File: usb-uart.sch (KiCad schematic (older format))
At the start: 11 parts

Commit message: sch: Add misc doc texts
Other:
- note added: "Connect both USB data pins despite\nthe stubs it will create: at USB 2.0\nspeeds, this is not really an issue"
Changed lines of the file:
@@
 Wire Wire Line
 	3150 4550 3300 4550
+Text Notes 3500 5100 0    50   ~ 0
+Connect both USB data pins despite\nthe stubs it will create: at USB 2.0\nspeeds, this is not really an issue
 $EndSCHEMATC

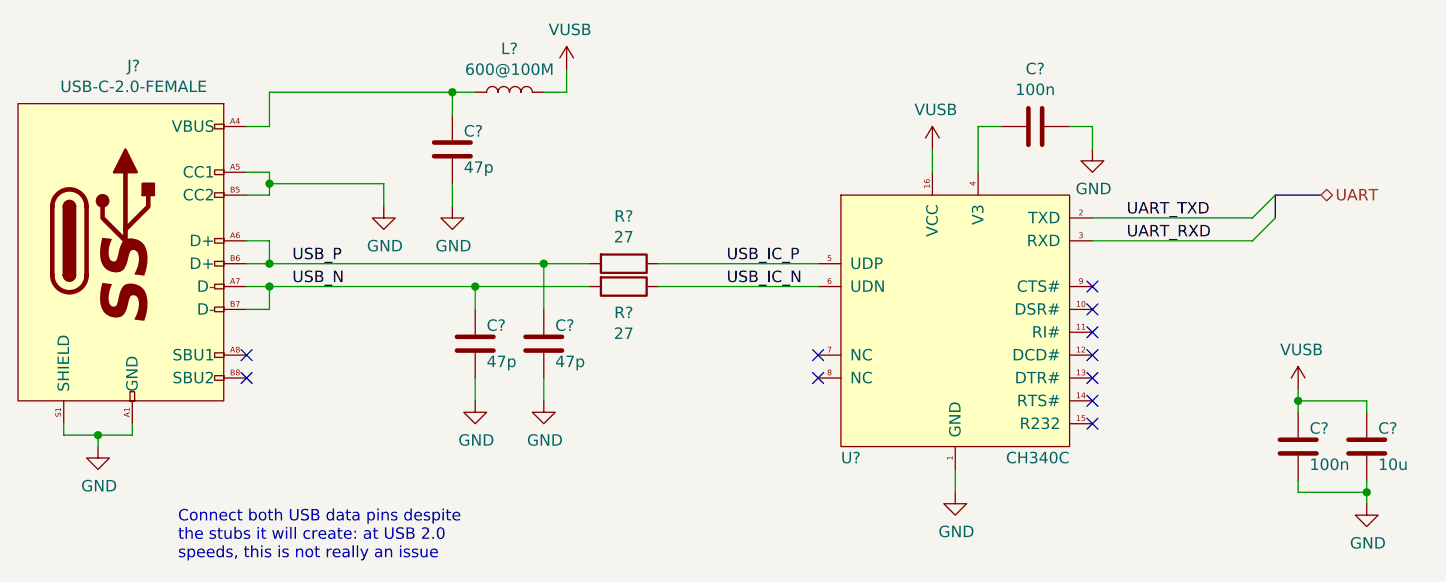
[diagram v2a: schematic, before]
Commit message: sch: Replace regular symbols with small variant
Done for most capacitors and resistors
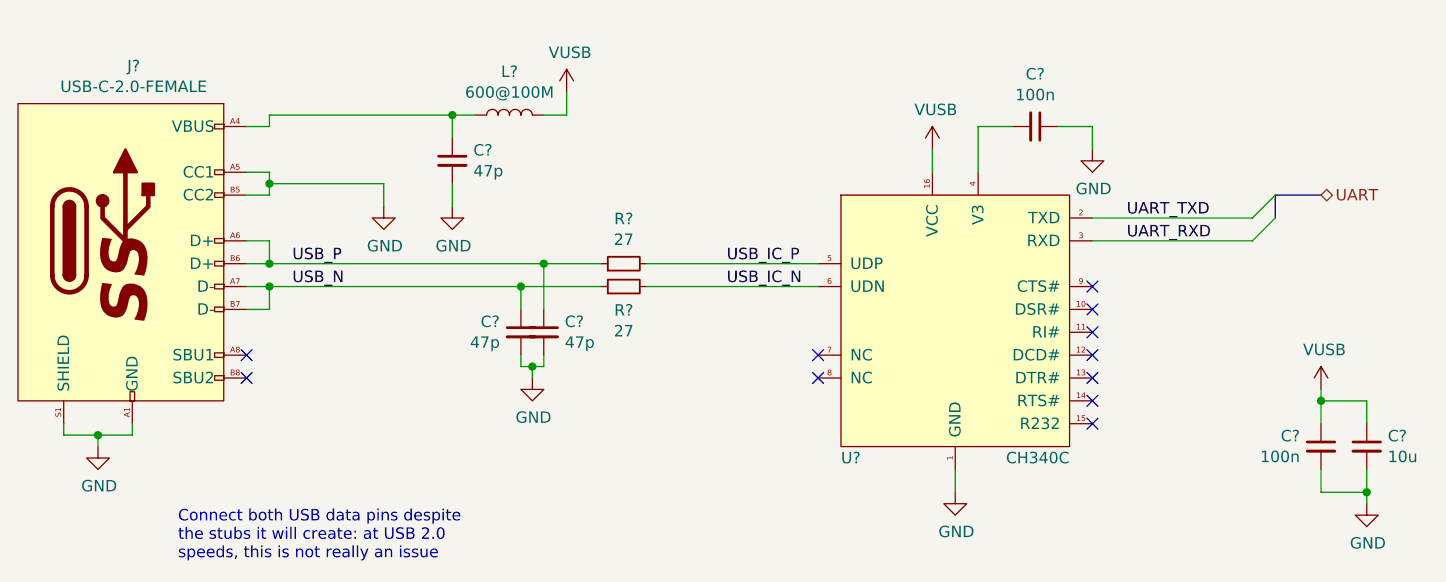
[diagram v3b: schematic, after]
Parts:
- removed C? (x2): 100n, symbol Device:C
- removed C? (x3): 47p, symbol Device:C
- removed C?: 10u, symbol Device:C
- removed R? (x2): 27, symbol Device:R
- added C? (x3): 47p, symbol Device:C_Small
- added C? (x2): 100n, symbol Device:C_Small
- added C?: 10u, symbol Device:C_Small
- added R? (x2): 27, symbol Device:R_Small
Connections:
- net GND: now also C?.1, C?.2, C?.2, C?.2, C?.2, C?.2
- net USB_IC_N: now also R?.2
- net USB_IC_P: now also R?.2
- net USB_N: now also C?.1, R?.1
- net USB_P: now also C?.1, R?.1
- net VUSB: now also C?.1, C?.1
- net at U?.4 (V3): now also C?.2
- net at J?.A4 (VBUS), J?.A9 (VBUS), J?.B4 (VBUS)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: now also C?.1
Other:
- moved on the sheet: L?
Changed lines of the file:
@@
 Wire Wire Line
 	6800 3300 6800 3400
-$Comp
-L Device:C C?
-U 1 1 5D27AF80
-P 7250 3200
-F 0 "C?" V 6998 3200 50  0000 C CNN
-F 1 "100n" V 7089 3200 50  0000 C CNN
-F 2 "" H 7288 3050 50  0001 C CNN
-F 3 "~" H 7250 3200 50  0001 C CNN
-	1    7250 3200
-	0    1    1    0
-$EndComp
 Wire Wire Line
 	7000 3400 7000 3200
-Wire Wire Line
-	7000 3200 7100 3200
 $Comp
 L power:GND #PWR?
@@
 	1    0    0    -1
 $EndComp
-Wire Wire Line
-	7400 3200 7500 3200
 Wire Wire Line
 	7500 3200 7500 3300
@@
 	1    0    0    -1
 $EndComp
-$Comp
-L Device:R R?
-U 1 1 5D27BD30
-P 5450 3800
-F 0 "R?" V 5243 3800 50  0000 C CNN
-F 1 "27" V 5334 3800 50  0000 C CNN
-F 2 "" V 5380 3800 50  0001 C CNN
-F 3 "~" H 5450 3800 50  0001 C CNN
-	1    5450 3800
-	0    1    1    0
-$EndComp
-$Comp
-L Device:R R?
-U 1 1 5D27BE5B
-P 5450 3900
-F 0 "R?" V 5565 3900 50  0000 C CNN
-F 1 "27" V 5656 3900 50  0000 C CNN
-F 2 "" V 5380 3900 50  0001 C CNN
-F 3 "~" H 5450 3900 50  0001 C CNN
-	1    5450 3900
-	0    1    1    0
-$EndComp
-Wire Wire Line
-	5600 3800 6300 3800
-Wire Wire Line
-	6300 3900 5600 3900
-Wire Wire Line
-	5300 3800 5100 3800
+Wire Wire Line
+	5550 3800 6300 3800
+Wire Wire Line
+	6300 3900 5550 3900
+Wire Wire Line
+	5350 3800 5100 3800
 Wire Wire Line
 	3800 3900 3900 3900
@@
 	3900 4000 3800 4000
 Connection ~ 3900 3900
-Wire Wire Line
-	3900 3900 4800 3900
 Text Label 5900 3800 0    50   ~ 0
 USB_IC_P
@@
 NoConn ~ 7500 4400
 NoConn ~ 7500 4500
-$Comp
-L Device:C C?
-U 1 1 5D27E126
-P 5100 4150
-F 0 "C?" H 5050 4100 50  0000 R TNN
-F 1 "47p" H 5050 4200 50  0000 R BNN
-F 2 "" H 5138 4000 50  0001 C CNN
-F 3 "~" H 5100 4150 50  0001 C CNN
-	1    5100 4150
-	-1   0    0    1
-$EndComp
-$Comp
-L Device:C C?
-U 1 1 5D27E3AF
-P 4800 4150
-F 0 "C?" H 4750 4100 50  0000 R TNN
-F 1 "47p" H 4750 4200 50  0000 R BNN
-F 2 "" H 4838 4000 50  0001 C CNN
-F 3 "~" H 4800 4150 50  0001 C CNN
-	1    4800 4150
-	-1   0    0    1
-$EndComp
 Wire Wire Line
 	5100 4000 5100 3800
@@
 	5100 3800 3900 3800
 Wire Wire Line
-	4800 4000 4800 3900
-Connection ~ 4800 3900
-Wire Wire Line
-	4800 3900 5300 3900
+	5000 4000 5000 3900
 $Comp
 L power:GND #PWR?
 U 1 1 5D27ED1B
-P 5100 4400
-F 0 "#PWR?" H 5100 4150 50  0001 C CNN
-F 1 "GND" H 5105 4227 50  0000 C CNN
-F 2 "" H 5100 4400 50  0001 C CNN
-F 3 "" H 5100 4400 50  0001 C CNN
-	1    5100 4400
-	1    0    0    -1
-$EndComp
-$Comp
-L power:GND #PWR?
-U 1 1 5D27ED34
-P 4800 4400
-F 0 "#PWR?" H 4800 4150 50  0001 C CNN
-F 1 "GND" H 4805 4227 50  0000 C CNN
-F 2 "" H 4800 4400 50  0001 C CNN
-F 3 "" H 4800 4400 50  0001 C CNN
-	1    4800 4400
-	1    0    0    -1
-$EndComp
-Wire Wire Line
-	4800 4300 4800 4400
-Wire Wire Line
-	5100 4300 5100 4400
+P 5050 4300
+F 0 "#PWR?" H 5050 4050 50  0001 C CNN
+F 1 "GND" H 5055 4127 50  0000 C CNN
+F 2 "" H 5050 4300 50  0001 C CNN
+F 3 "" H 5050 4300 50  0001 C CNN
+	1    5050 4300
+	1    0    0    -1
+$EndComp
+Wire Wire Line
+	5000 4200 5000 4250
+Wire Wire Line
+	5100 4200 5100 4250
 Wire Wire Line
 	3300 4500 3300 4550
@@
 L Device:L L?
 U 1 1 5D2813FA
-P 4950 3050
+P 4950 3150
 AR Path="/5C7D0D1E/5C7D3CAF/5D2813FA" Ref="L?"  Part="1"
 AR Path="/5C7D0D1E/5C7D3CB2/5D2813FA" Ref="L?"  Part="1"
 AR Path="/5D2774DB/5D2813FA" Ref="L?"  Part="1"
-F 0 "L?" V 5140 3050 50  0000 C CNN
-F 1 "600@100M" V 5049 3050 50  0000 C CNN
-F 2 "" H 4950 3050 50  0001 C CNN
-F 3 "~" H 4950 3050 50  0001 C CNN
-	1    4950 3050
+F 0 "L?" V 5140 3150 50  0000 C CNN
+F 1 "600@100M" V 5049 3150 50  0000 C CNN
+F 2 "" H 4950 3150 50  0001 C CNN
+F 3 "~" H 4950 3150 50  0001 C CNN
+	1    4950 3150
 	0    -1   -1   0
 $EndComp
-$Comp
-L Device:C C?
-U 1 1 5D281882
-P 4700 3300
-F 0 "C?" H 4650 3250 50  0000 R TNN
-F 1 "47p" H 4650 3350 50  0000 R BNN
-F 2 "" H 4738 3150 50  0001 C CNN
-F 3 "~" H 4700 3300 50  0001 C CNN
-	1    4700 3300
-	-1   0    0    1
-$EndComp
-Wire Wire Line
-	3900 3200 3900 3050
-Wire Wire Line
-	3900 3050 4700 3050
+Wire Wire Line
+	3900 3200 3900 3150
 Wire Wire Line
 	3800 3200 3900 3200
-Wire Wire Line
-	4700 3150 4700 3050
-Connection ~ 4700 3050
-Wire Wire Line
-	4700 3050 4800 3050
 $Comp
 L power:GND #PWR?
@@
 L pimouss-motherboard:VUSB #PWR?
 U 1 1 5D2857EF
-P 5200 2950
-F 0 "#PWR?" H 5200 2800 50  0001 C CNN
-F 1 "VUSB" H 5215 3123 50  0000 C CNN
-F 2 "" H 5200 2950 50  0001 C CNN
-F 3 "" H 5200 2950 50  0001 C CNN
-	1    5200 2950
-	1    0    0    -1
-$EndComp
-Wire Wire Line
-	5100 3050 5200 3050
-Wire Wire Line
-	5200 3050 5200 2950
-$Comp
-L Device:C C?
-U 1 1 5D2868CF
-P 8700 4600
-F 0 "C?" H 8650 4550 50  0000 R TNN
-F 1 "10u" H 8650 4650 50  0000 R BNN
-F 2 "" H 8738 4450 50  0001 C CNN
-F 3 "~" H 8700 4600 50  0001 C CNN
-	1    8700 4600
-	-1   0    0    1
-$EndComp
-$Comp
-L Device:C C?
-U 1 1 5D2868D6
-P 8400 4600
-F 0 "C?" H 8350 4550 50  0000 R TNN
-F 1 "100n" H 8350 4650 50  0000 R BNN
-F 2 "" H 8438 4450 50  0001 C CNN
-F 3 "~" H 8400 4600 50  0001 C CNN
-	1    8400 4600
-	-1   0    0    1
-$EndComp
+P 5200 3050
+F 0 "#PWR?" H 5200 2900 50  0001 C CNN
+F 1 "VUSB" H 5215 3223 50  0000 C CNN
+F 2 "" H 5200 3050 50  0001 C CNN
+F 3 "" H 5200 3050 50  0001 C CNN
+	1    5200 3050
+	1    0    0    -1
+$EndComp
+Wire Wire Line
+	5100 3150 5200 3150
+Wire Wire Line
+	5200 3150 5200 3050
 $Comp
 L pimouss-motherboard:VUSB #PWR?
 U 1 1 5D286FE7
-P 8400 4350
-F 0 "#PWR?" H 8400 4200 50  0001 C CNN
-F 1 "VUSB" H 8415 4523 50  0000 C CNN
-F 2 "" H 8400 4350 50  0001 C CNN
-F 3 "" H 8400 4350 50  0001 C CNN
-	1    8400 4350
+P 8500 4350
+F 0 "#PWR?" H 8500 4200 50  0001 C CNN
+F 1 "VUSB" H 8515 4523 50  0000 C CNN
+F 2 "" H 8500 4350 50  0001 C CNN
+F 3 "" H 8500 4350 50  0001 C CNN
+	1    8500 4350
 	1    0    0    -1
 $EndComp
@@
 $EndComp
 Wire Wire Line
-	8400 4350 8400 4400
-Wire Wire Line
-	8400 4400 8700 4400
-Wire Wire Line
-	8700 4400 8700 4450
-Connection ~ 8400 4400
-Wire Wire Line
-	8400 4400 8400 4450
-Wire Wire Line
-	8400 4750 8400 4800
-Wire Wire Line
-	8400 4800 8700 4800
+	8500 4350 8500 4400
+Wire Wire Line
+	8500 4400 8700 4400
+Wire Wire Line
+	8700 4400 8700 4500
+Connection ~ 8500 4400
+Wire Wire Line
+	8500 4400 8500 4500
+Wire Wire Line
+	8500 4700 8500 4800
+Wire Wire Line
+	8500 4800 8700 4800
 Wire Wire Line
 	8700 4800 8700 4850
 Wire Wire Line
-	8700 4750 8700 4800
+	8700 4700 8700 4800
 Connection ~ 8700 4800
 Wire Wire Line
@@
 Text Notes 3500 5100 0    50   ~ 0
 Connect both USB data pins despite\nthe stubs it will create: at USB 2.0\nspeeds, this is not really an issue
+$Comp
+L Device:R_Small R?
+U 1 1 5D489A44
+P 5450 3800
+F 0 "R?" V 5646 3800 50  0000 C CNN
+F 1 "27" V 5555 3800 50  0000 C CNN
+F 2 "" H 5450 3800 50  0001 C CNN
+F 3 "~" H 5450 3800 50  0001 C CNN
+	1    5450 3800
+	0    -1   -1   0
+$EndComp
+$Comp
+L Device:C_Small C?
+U 1 1 5D48AA53
+P 4700 3350
+F 0 "C?" H 4792 3396 50  0000 L CNN
+F 1 "47p" H 4792 3305 50  0000 L CNN
+F 2 "" H 4700 3350 50  0001 C CNN
+F 3 "~" H 4700 3350 50  0001 C CNN
+	1    4700 3350
+	1    0    0    -1
+$EndComp
+Wire Wire Line
+	4700 3250 4700 3150
+Wire Wire Line
+	3900 3150 4700 3150
+Connection ~ 4700 3150
+Wire Wire Line
+	4700 3150 4800 3150
+$Comp
+L Device:R_Small R?
+U 1 1 5D491922
+P 5450 3900
+F 0 "R?" V 5346 3900 50  0000 C CNN
+F 1 "27" V 5255 3900 50  0000 C CNN
+F 2 "" H 5450 3900 50  0001 C CNN
+F 3 "~" H 5450 3900 50  0001 C CNN
+	1    5450 3900
+	0    -1   -1   0
+$EndComp
+$Comp
+L Device:C_Small C?
+U 1 1 5D493D2D
+P 5100 4100
+F 0 "C?" H 5192 4146 50  0000 L CNN
+F 1 "47p" H 5192 4055 50  0000 L CNN
+F 2 "" H 5100 4100 50  0001 C CNN
+F 3 "~" H 5100 4100 50  0001 C CNN
+	1    5100 4100
+	1    0    0    -1
+$EndComp
+$Comp
+L Device:C_Small C?
+U 1 1 5D495256
+P 5000 4100
+F 0 "C?" H 4908 4146 50  0000 R CNN
+F 1 "47p" H 4908 4055 50  0000 R CNN
+F 2 "" H 5000 4100 50  0001 C CNN
+F 3 "~" H 5000 4100 50  0001 C CNN
+	1    5000 4100
+	1    0    0    -1
+$EndComp
+Connection ~ 5000 3900
+Wire Wire Line
+	5000 3900 5350 3900
+Wire Wire Line
+	3900 3900 5000 3900
+Wire Wire Line
+	5000 4250 5050 4250
+Wire Wire Line
+	5050 4250 5050 4300
+Connection ~ 5050 4250
+Wire Wire Line
+	5050 4250 5100 4250
+$Comp
+L Device:C_Small C?
+U 1 1 5D4A0412
+P 7250 3200
+F 0 "C?" V 7021 3200 50  0000 C CNN
+F 1 "100n" V 7112 3200 50  0000 C CNN
+F 2 "" H 7250 3200 50  0001 C CNN
+F 3 "~" H 7250 3200 50  0001 C CNN
+	1    7250 3200
+	0    1    1    0
+$EndComp
+Wire Wire Line
+	7000 3200 7150 3200
+Wire Wire Line
+	7350 3200 7500 3200
+$Comp
+L Device:C_Small C?
+U 1 1 5D4A5872
+P 8500 4600
+F 0 "C?" H 8408 4646 50  0000 R CNN
+F 1 "100n" H 8408 4555 50  0000 R CNN
+F 2 "" H 8500 4600 50  0001 C CNN
+F 3 "~" H 8500 4600 50  0001 C CNN
+	1    8500 4600
+	1    0    0    -1
+$EndComp
+$Comp
+L Device:C_Small C?
+U 1 1 5D4A64DB
+P 8700 4600
+F 0 "C?" H 8792 4646 50  0000 L CNN
+F 1 "10u" H 8792 4555 50  0000 L CNN
+F 2 "" H 8700 4600 50  0001 C CNN
+F 3 "~" H 8700 4600 50  0001 C CNN
+	1    8700 4600
+	1    0    0    -1
+$EndComp
 $EndSCHEMATC

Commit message: sch: Remove ALL busses since kicad's support is broken
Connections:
- net UART_RXD renamed RXD
- net UART_TXD renamed TXD
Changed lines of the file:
@@
 	8200 3700 7500 3700
 Text Label 7650 3600 0    50   ~ 0
-UART_TXD
+TXD
 Text Label 7650 3700 0    50   ~ 0
-UART_RXD
-Wire Bus Line
-	8300 3600 8300 3500
-Wire Bus Line
-	8300 3500 8500 3500
-Entry Wire Line
-	8200 3600 8300 3500
-Entry Wire Line
-	8200 3700 8300 3600
-Text HLabel 8500 3500 2    50   BiDi ~ 0
-UART
+RXD
 Wire Wire Line
 	3900 3450 4400 3450
@@
 	1    0    0    -1
 $EndComp
+Text HLabel 8200 3600 2    50   Output ~ 0
+TXD
+Text HLabel 8200 3700 2    50   Input ~ 0
+RXD
 $EndSCHEMATC

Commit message: sch: Make ERC happy with dummy power outputs
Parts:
- added DS?: DummySupply, symbol pimouss-motherboard:DummySupply
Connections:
- net VUSB: now also DS?.~ (Dummy)
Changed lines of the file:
@@
 Text HLabel 8200 3700 2    50   Input ~ 0
 RXD
+$Comp
+L pimouss-motherboard:DummySupply DS?
+U 1 1 5E40E77B
+P 5200 3150
+F 0 "DS?" H 5200 3150 50  0001 C CNN
+F 1 "DummySupply" H 5200 3150 50  0001 C CNN
+F 2 "" H 5200 3150 50  0001 C CNN
+F 3 "" H 5200 3150 50  0001 C CNN
+	1    5200 3150
+	0    1    1    0
+$EndComp
+Connection ~ 5200 3150
 $EndSCHEMATC

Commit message: sch: Annotate & associate symbols with footprints
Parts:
- removed DS?: DummySupply, symbol pimouss-motherboard:DummySupply
- C34, C35, C36, C37, C38, C39: renamed from C?; footprint (none) -> Capacitor_SMD:C_0603_1608Metric
- L7: renamed from L?; footprint (none) -> Inductor_SMD:L_0603_1608Metric
- R44, R45: renamed from R?; footprint (none) -> Resistor_SMD:R_0603_1608Metric
- gave numbers to parts that had none: 2
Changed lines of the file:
@@
 $EndDescr
 $Comp
-L power:GND #PWR?
+L power:GND #PWR086
 U 1 1 5D2776A6
 P 6900 4800
-F 0 "#PWR?" H 6900 4550 50  0001 C CNN
+F 0 "#PWR086" H 6900 4550 50  0001 C CNN
 F 1 "GND" H 6905 4627 50  0000 C CNN
 F 2 "" H 6900 4800 50  0001 C CNN
@@
 	6900 4700 6900 4800
 $Comp
-L pimouss-motherboard:CH340C U?
+L pimouss-motherboard:CH340C U6
 U 1 1 5D2790CD
 P 6400 3500
-F 0 "U?" H 6400 2350 50  0000 L CNN
+F 0 "U6" H 6400 2350 50  0000 L CNN
 F 1 "CH340C" H 7400 2350 50  0000 R CNN
 F 2 "Package_SO:SSOP-20_5.3x7.2mm_P0.65mm" H 7300 1950 50  0001 C CNN
@@
 $EndComp
 $Comp
-L pimouss-motherboard:VUSB #PWR?
+L pimouss-motherboard:VUSB #PWR085
 U 1 1 5D27A4FA
 P 6800 3300
-F 0 "#PWR?" H 6800 3150 50  0001 C CNN
+F 0 "#PWR085" H 6800 3150 50  0001 C CNN
 F 1 "VUSB" H 6815 3473 50  0000 C CNN
 F 2 "" H 6800 3300 50  0001 C CNN
@@
 	7000 3400 7000 3200
 $Comp
-L power:GND #PWR?
+L power:GND #PWR087
 U 1 1 5D27B04F
 P 7500 3300
-F 0 "#PWR?" H 7500 3050 50  0001 C CNN
+F 0 "#PWR087" H 7500 3050 50  0001 C CNN
 F 1 "GND" H 7505 3127 50  0000 C CNN
 F 2 "" H 7500 3300 50  0001 C CNN
@@
 	7500 3200 7500 3300
 $Comp
-L pimouss-motherboard:USB-C-2.0-FEMALE J?
+L pimouss-motherboard:USB-C-2.0-FEMALE J5
 U 1 1 5D27BBAF
 P 2800 3100
-F 0 "J?" H 3306 3265 50  0000 C CNN
+F 0 "J5" H 3306 3265 50  0000 C CNN
 F 1 "USB-C-2.0-FEMALE" H 3306 3174 50  0000 C CNN
 F 2 "pimouss-motherboard:USB-C-FEMALE" H 3550 1600 50  0001 C CNN
@@
 	5000 4000 5000 3900
 $Comp
-L power:GND #PWR?
+L power:GND #PWR083
 U 1 1 5D27ED1B
 P 5050 4300
-F 0 "#PWR?" H 5050 4050 50  0001 C CNN
+F 0 "#PWR083" H 5050 4050 50  0001 C CNN
 F 1 "GND" H 5055 4127 50  0000 C CNN
 F 2 "" H 5050 4300 50  0001 C CNN
@@
 Connection ~ 3900 3450
 $Comp
-L power:GND #PWR?
+L power:GND #PWR081
 U 1 1 5D280DF4
 P 4400 3550
-F 0 "#PWR?" H 4400 3300 50  0001 C CNN
+F 0 "#PWR081" H 4400 3300 50  0001 C CNN
 F 1 "GND" H 4405 3377 50  0000 C CNN
 F 2 "" H 4400 3550 50  0001 C CNN
@@
 AR Path="/5C7D0D1E/5C7D3CAF/5D2813FA" Ref="L?"  Part="1"
 AR Path="/5C7D0D1E/5C7D3CB2/5D2813FA" Ref="L?"  Part="1"
-AR Path="/5D2774DB/5D2813FA" Ref="L?"  Part="1"
-F 0 "L?" V 5140 3150 50  0000 C CNN
+AR Path="/5D2774DB/5D2813FA" Ref="L7"  Part="1"
+F 0 "L7" V 5140 3150 50  0000 C CNN
 F 1 "600@100M" V 5049 3150 50  0000 C CNN
-F 2 "" H 4950 3150 50  0001 C CNN
+F 2 "Inductor_SMD:L_0603_1608Metric" H 4950 3150 50  0001 C CNN
 F 3 "~" H 4950 3150 50  0001 C CNN
 	1    4950 3150
@@
 	3800 3200 3900 3200
 $Comp
-L power:GND #PWR?
+L power:GND #PWR082
 U 1 1 5D284FF6
 P 4700 3550
-F 0 "#PWR?" H 4700 3300 50  0001 C CNN
+F 0 "#PWR082" H 4700 3300 50  0001 C CNN
 F 1 "GND" H 4705 3377 50  0000 C CNN
 F 2 "" H 4700 3550 50  0001 C CNN
@@
 	4700 3450 4700 3550
 $Comp
-L pimouss-motherboard:VUSB #PWR?
+L pimouss-motherboard:VUSB #PWR084
 U 1 1 5D2857EF
 P 5200 3050
-F 0 "#PWR?" H 5200 2900 50  0001 C CNN
+F 0 "#PWR084" H 5200 2900 50  0001 C CNN
 F 1 "VUSB" H 5215 3223 50  0000 C CNN
 F 2 "" H 5200 3050 50  0001 C CNN
@@
 	5200 3150 5200 3050
 $Comp
-L pimouss-motherboard:VUSB #PWR?
+L pimouss-motherboard:VUSB #PWR088
 U 1 1 5D286FE7
 P 8500 4350
-F 0 "#PWR?" H 8500 4200 50  0001 C CNN
+F 0 "#PWR088" H 8500 4200 50  0001 C CNN
 F 1 "VUSB" H 8515 4523 50  0000 C CNN
 F 2 "" H 8500 4350 50  0001 C CNN
@@
 $EndComp
 $Comp
-L power:GND #PWR?
+L power:GND #PWR089
 U 1 1 5D287011
 P 8700 4850
-F 0 "#PWR?" H 8700 4600 50  0001 C CNN
+F 0 "#PWR089" H 8700 4600 50  0001 C CNN
 F 1 "GND" H 8705 4677 50  0000 C CNN
 F 2 "" H 8700 4850 50  0001 C CNN
@@
 	3000 4550 3150 4550
 $Comp
-L power:GND #PWR?
+L power:GND #PWR080
 U 1 1 5D29968A
 P 3150 4600
-F 0 "#PWR?" H 3150 4350 50  0001 C CNN
+F 0 "#PWR080" H 3150 4350 50  0001 C CNN
 F 1 "GND" H 3155 4427 50  0000 C CNN
 F 2 "" H 3150 4600 50  0001 C CNN
@@
 Connect both USB data pins despite\nthe stubs it will create: at USB 2.0\nspeeds, this is not really an issue
 $Comp
-L Device:R_Small R?
+L Device:R_Small R44
 U 1 1 5D489A44
 P 5450 3800
-F 0 "R?" V 5646 3800 50  0000 C CNN
+F 0 "R44" V 5646 3800 50  0000 C CNN
 F 1 "27" V 5555 3800 50  0000 C CNN
-F 2 "" H 5450 3800 50  0001 C CNN
+F 2 "Resistor_SMD:R_0603_1608Metric" H 5450 3800 50  0001 C CNN
 F 3 "~" H 5450 3800 50  0001 C CNN
 	1    5450 3800
@@
 $EndComp
 $Comp
-L Device:C_Small C?
+L Device:C_Small C34
 U 1 1 5D48AA53
 P 4700 3350
-F 0 "C?" H 4792 3396 50  0000 L CNN
+F 0 "C34" H 4792 3396 50  0000 L CNN
 F 1 "47p" H 4792 3305 50  0000 L CNN
-F 2 "" H 4700 3350 50  0001 C CNN
+F 2 "Capacitor_SMD:C_0603_1608Metric" H 4700 3350 50  0001 C CNN
 F 3 "~" H 4700 3350 50  0001 C CNN
 	1    4700 3350
@@
 	4700 3150 4800 3150
 $Comp
-L Device:R_Small R?
+L Device:R_Small R45
 U 1 1 5D491922
 P 5450 3900
-F 0 "R?" V 5346 3900 50  0000 C CNN
+F 0 "R45" V 5346 3900 50  0000 C CNN
 F 1 "27" V 5255 3900 50  0000 C CNN
-F 2 "" H 5450 3900 50  0001 C CNN
+F 2 "Resistor_SMD:R_0603_1608Metric" H 5450 3900 50  0001 C CNN
 F 3 "~" H 5450 3900 50  0001 C CNN
 	1    5450 3900
@@
 $EndComp
 $Comp
-L Device:C_Small C?
+L Device:C_Small C36
 U 1 1 5D493D2D
 P 5100 4100
-F 0 "C?" H 5192 4146 50  0000 L CNN
+F 0 "C36" H 5192 4146 50  0000 L CNN
 F 1 "47p" H 5192 4055 50  0000 L CNN
-F 2 "" H 5100 4100 50  0001 C CNN
+F 2 "Capacitor_SMD:C_0603_1608Metric" H 5100 4100 50  0001 C CNN
 F 3 "~" H 5100 4100 50  0001 C CNN
 	1    5100 4100
@@
 $EndComp
 $Comp
-L Device:C_Small C?
+L Device:C_Small C35
 U 1 1 5D495256
 P 5000 4100
-F 0 "C?" H 4908 4146 50  0000 R CNN
+F 0 "C35" H 4908 4146 50  0000 R CNN
 F 1 "47p" H 4908 4055 50  0000 R CNN
-F 2 "" H 5000 4100 50  0001 C CNN
+F 2 "Capacitor_SMD:C_0603_1608Metric" H 5000 4100 50  0001 C CNN
 F 3 "~" H 5000 4100 50  0001 C CNN
 	1    5000 4100
@@
 	5050 4250 5100 4250
 $Comp
-L Device:C_Small C?
+L Device:C_Small C37
 U 1 1 5D4A0412
 P 7250 3200
-F 0 "C?" V 7021 3200 50  0000 C CNN
+F 0 "C37" V 7021 3200 50  0000 C CNN
 F 1 "100n" V 7112 3200 50  0000 C CNN
-F 2 "" H 7250 3200 50  0001 C CNN
+F 2 "Capacitor_SMD:C_0603_1608Metric" H 7250 3200 50  0001 C CNN
 F 3 "~" H 7250 3200 50  0001 C CNN
 	1    7250 3200
@@
 	7350 3200 7500 3200
 $Comp
-L Device:C_Small C?
+L Device:C_Small C38
 U 1 1 5D4A5872
 P 8500 4600
-F 0 "C?" H 8408 4646 50  0000 R CNN
+F 0 "C38" H 8408 4646 50  0000 R CNN
 F 1 "100n" H 8408 4555 50  0000 R CNN
-F 2 "" H 8500 4600 50  0001 C CNN
+F 2 "Capacitor_SMD:C_0603_1608Metric" H 8500 4600 50  0001 C CNN
 F 3 "~" H 8500 4600 50  0001 C CNN
 	1    8500 4600
@@
 $EndComp
 $Comp
-L Device:C_Small C?
+L Device:C_Small C39
 U 1 1 5D4A64DB
 P 8700 4600
-F 0 "C?" H 8792 4646 50  0000 L CNN
+F 0 "C39" H 8792 4646 50  0000 L CNN
 F 1 "10u" H 8792 4555 50  0000 L CNN
-F 2 "" H 8700 4600 50  0001 C CNN
+F 2 "Capacitor_SMD:C_0603_1608Metric" H 8700 4600 50  0001 C CNN
 F 3 "~" H 8700 4600 50  0001 C CNN
 	1    8700 4600
@@
 RXD
 $Comp
-L pimouss-motherboard:DummySupply DS?
+L pimouss-motherboard:DummySupply #DS011
 U 1 1 5E40E77B
 P 5200 3150
-F 0 "DS?" H 5200 3150 50  0001 C CNN
+F 0 "#DS011" H 5200 3150 50  0001 C CNN
 F 1 "DummySupply" H 5200 3150 50  0001 C CNN
 F 2 "" H 5200 3150 50  0001 C CNN

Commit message: lib, sch: Fix connectors refdes letter
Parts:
- renumbered J5 to P5, U6 to U3
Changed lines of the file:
@@
 	6900 4700 6900 4800
 $Comp
-L pimouss-motherboard:CH340C U6
+L pimouss-motherboard:CH340C U3
 U 1 1 5D2790CD
 P 6400 3500
-F 0 "U6" H 6400 2350 50  0000 L CNN
+F 0 "U3" H 6400 2350 50  0000 L CNN
 F 1 "CH340C" H 7400 2350 50  0000 R CNN
 F 2 "Package_SO:SSOP-20_5.3x7.2mm_P0.65mm" H 7300 1950 50  0001 C CNN
@@
 	7500 3200 7500 3300
 $Comp
-L pimouss-motherboard:USB-C-2.0-FEMALE J5
+L pimouss-motherboard:USB-C-2.0-FEMALE P5
 U 1 1 5D27BBAF
 P 2800 3100
-F 0 "J5" H 3306 3265 50  0000 C CNN
+F 0 "P5" H 3306 3265 50  0000 C CNN
 F 1 "USB-C-2.0-FEMALE" H 3306 3174 50  0000 C CNN
 F 2 "pimouss-motherboard:USB-C-FEMALE" H 3550 1600 50  0001 C CNN
